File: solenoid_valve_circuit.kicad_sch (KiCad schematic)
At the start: 5 parts, among them J3 436500201, Q1 NMOS

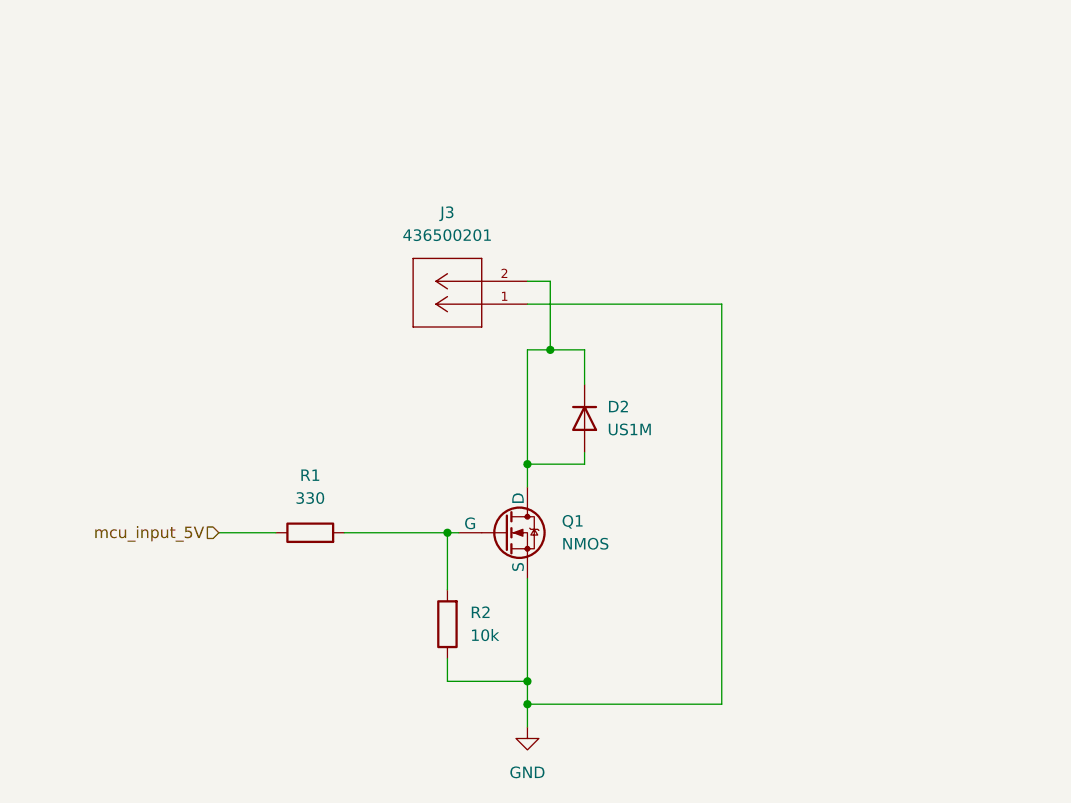
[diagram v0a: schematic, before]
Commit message: added npn in so that GPIO can be 5V or roughly 0V
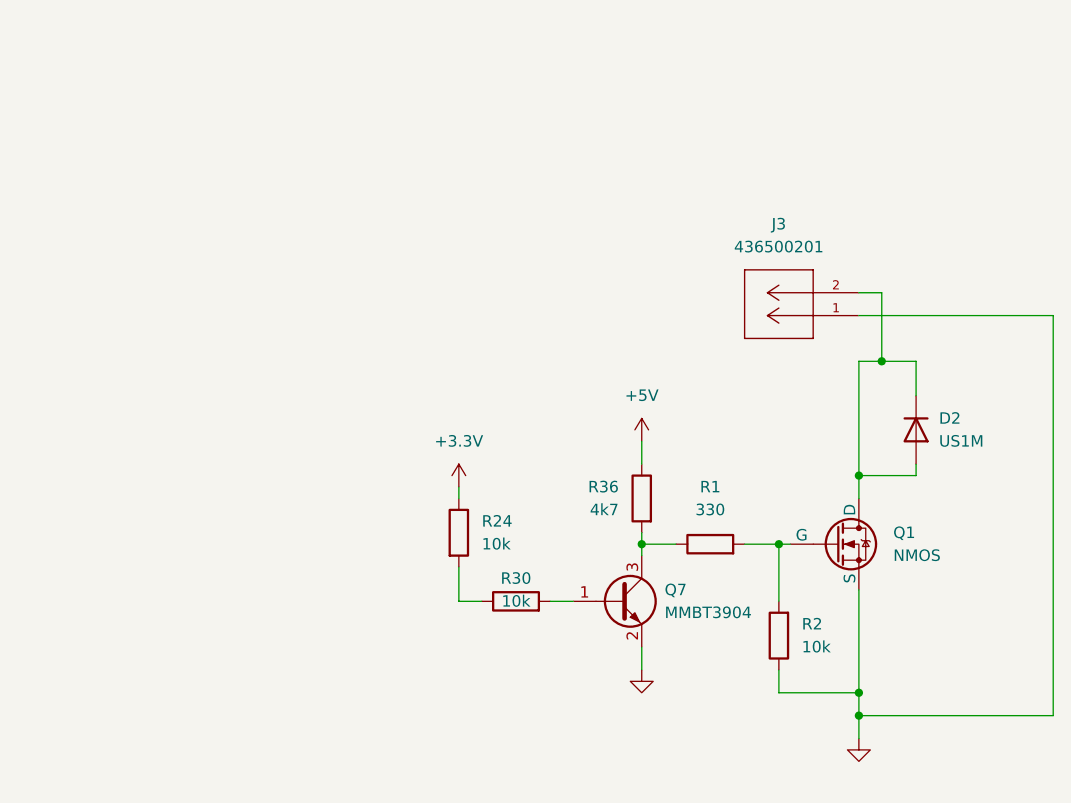
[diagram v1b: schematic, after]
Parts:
- added Q7: MMBT3904, Package_TO_SOT_SMD:SOT-23, symbol Transistor_BJT:MMBT3904
- added R24, R30: 10k, symbol Device:R
- added R36: 4k7, symbol Device:R
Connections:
- net GND: now also Q7.2 (E)
- net mcu_input_5V: no longer names the net of R1.1
- net mcu_input_5V: now also Q7.3 (C), R36.2
- new net: R24.2, R30.1
- new net: Q7.1 (B), R30.2
- new net +3.3V: R24.1
- new net +5V: R36.1
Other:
- moved on the sheet: D2, J3, Q1, R1, R2

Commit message: Added changes to pass ERC check
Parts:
- R19: renamed from R2; value 10k -> 100k
- renumbered D2 to D1, J3 to J4, Q7 to Q1, Q1 to Q2, R24 to R15, R30 to R16, R36 to R17, R1 to R18
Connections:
- net mcu_input_5V: now reaches R15.2, R16.1
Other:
- moved on the sheet: D1, J4, Q1, Q2, R15, R16, R17, R18, R19

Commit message: added footprints to every component except inductors. That will be in the next commit
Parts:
- R15, R16, R17, R18, R19: footprint (none) -> Resistor_SMD:R_0402_1005Metric
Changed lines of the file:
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@@
 			)
 		)
-		(property "Footprint" ""
+		(property "Footprint" "Resistor_SMD:R_0402_1005Metric"
 			(at 65.532 68.58 90)
 			(hide yes)
@@
 			)
 		)
-		(property "Footprint" ""
+		(property "Footprint" "Resistor_SMD:R_0402_1005Metric"
 			(at 73.66 77.978 90)
 			(hide yes)
@@
 			)
 		)
-		(property "Footprint" ""
+		(property "Footprint" "Resistor_SMD:R_0402_1005Metric"
 			(at 95.25 71.628 90)
 			(hide yes)
@@
 			)
 		)
-		(property "Footprint" ""
+		(property "Footprint" "Resistor_SMD:R_0402_1005Metric"
 			(at 89.408 64.77 90)
 			(hide yes)
@@
 			)
 		)
-		(property "Footprint" ""
+		(property "Footprint" "Resistor_SMD:R_0402_1005Metric"
 			(at 103.378 80.01 90)
 			(hide yes)
